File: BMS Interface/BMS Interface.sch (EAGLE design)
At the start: 23 parts

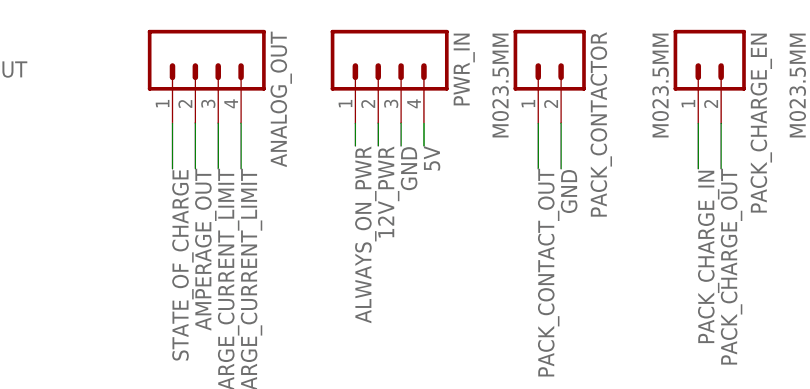
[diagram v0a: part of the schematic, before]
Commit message: Updating layout for BMS interface PCB and removed 5V input as it was no longer necessary.
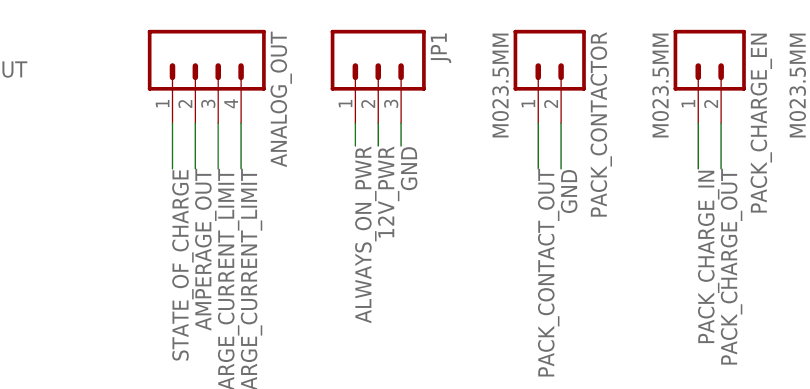
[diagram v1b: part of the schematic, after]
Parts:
- removed PWR_IN: (no value), SparkFun-Connectors:M04SCREW
- added JP1: (no value), SparkFun-Connectors:M03SCREW
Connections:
- removed net 5V: PWR_IN.4
- net 12V_PWR: now also JP1.2; no longer PWR_IN.2
- net ALWAYS_ON_PWR: now also JP1.1; no longer PWR_IN.1
- net GND: now also JP1.3; no longer PWR_IN.3
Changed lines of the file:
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@@
 <parts>
 <part name="BMS_IO" library="SparkFun-Connectors" deviceset="M13X2" device="2X13"/>
-<part name="PWR_IN" library="SparkFun-Connectors" deviceset="M04" device="SCREW"/>
 <part name="CAN1" library="SparkFun-Connectors" deviceset="DB9" device="FEMALE"/>
 <part name="CAN2" library="SparkFun-Connectors" deviceset="DB9" device="FEMALE"/>
@@
 <part name="STANDOFF3" library="SparkFun-Electromechanical" deviceset="STAND-OFF" device=""/>
 <part name="STANDOFF4" library="SparkFun-Electromechanical" deviceset="STAND-OFF" device=""/>
+<part name="JP1" library="SparkFun-Connectors" deviceset="M03" device="SCREW"/>
 </parts>
 <sheets>
@@
 <instances>
 <instance part="BMS_IO" gate="G$1" x="-2.54" y="50.8"/>
-<instance part="PWR_IN" gate="G$1" x="86.36" y="121.92" rot="R270"/>
 <instance part="CAN1" gate="G$1" x="124.46" y="43.18"/>
 <instance part="CAN2" gate="G$1" x="124.46" y="15.24"/>
@@
 <instance part="STANDOFF3" gate="G$1" x="160.02" y="68.58"/>
 <instance part="STANDOFF4" gate="G$1" x="160.02" y="71.12"/>
+<instance part="JP1" gate="G$1" x="86.36" y="124.46" rot="R270"/>
 </instances>
 <busses>
@@
 <wire x1="83.82" y1="116.84" x2="83.82" y2="114.3" width="0.2032" layer="91"/>
 <label x="83.82" y="114.3" size="1.778" layer="95" rot="R270"/>
-<pinref part="PWR_IN" gate="G$1" pin="1"/>
+<pinref part="JP1" gate="G$1" pin="1"/>
 </segment>
 </net>
@@
 <wire x1="88.9" y1="116.84" x2="88.9" y2="114.3" width="0.2032" layer="91"/>
 <label x="88.9" y="114.3" size="1.778" layer="95" rot="R270"/>
-<pinref part="PWR_IN" gate="G$1" pin="3"/>
+<pinref part="JP1" gate="G$1" pin="3"/>
 </segment>
 <segment>
@@
 <wire x1="86.36" y1="116.84" x2="86.36" y2="114.3" width="0.2032" layer="91"/>
 <label x="86.36" y="114.3" size="1.778" layer="95" rot="R270"/>
-<pinref part="PWR_IN" gate="G$1" pin="2"/>
+<pinref part="JP1" gate="G$1" pin="2"/>
 </segment>
 <segment>
@@
 </segment>
 </net>
-<net name="5V" class="0">
-<segment>
-<pinref part="PWR_IN" gate="G$1" pin="4"/>
-<wire x1="91.44" y1="116.84" x2="91.44" y2="114.3" width="0.2032" layer="91"/>
-<label x="91.44" y="114.3" size="1.778" layer="95" rot="R270"/>
-</segment>
-</net>

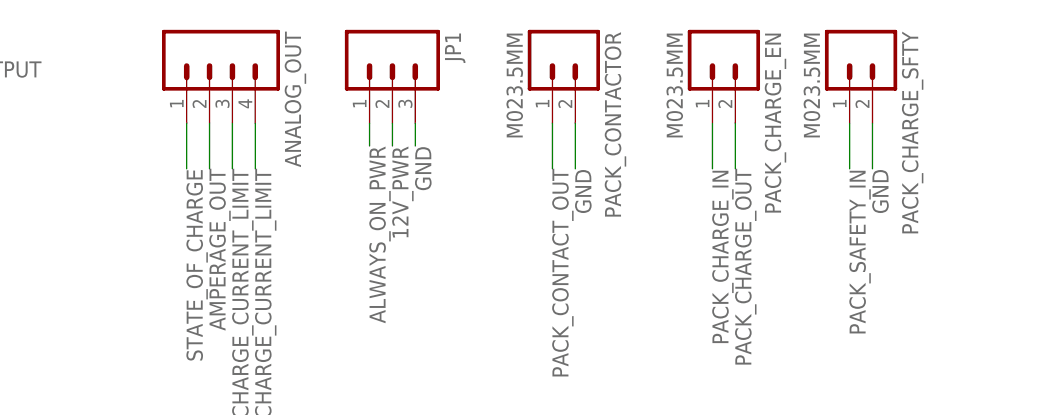
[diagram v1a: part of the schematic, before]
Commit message: CHanged all connectors on MCB to use Molex
Changed most of the connectors on the BMS interface to use molex as
well.
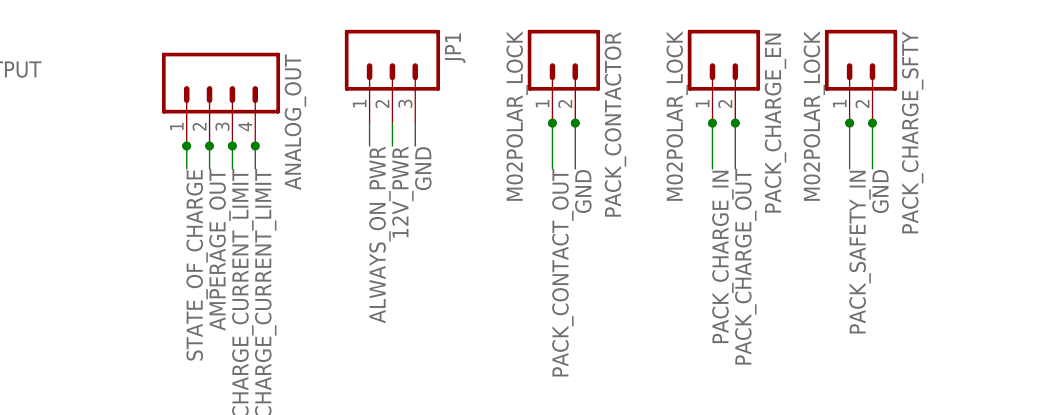
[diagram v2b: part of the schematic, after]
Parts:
- ANALOG_OUT: device SparkFun-Connectors:M04PTH -> SparkFun-Connectors:M04POLAR_LOCK
- PACK_CHARGE_EN, PACK_CHARGE_SFTY, PACK_CONTACTOR: value M023.5MM -> M02POLAR_LOCK; device SparkFun-Connectors:M023.5MM -> SparkFun-Connectors:M02POLAR_LOCK
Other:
- moved on the sheet: ANALOG_OUT
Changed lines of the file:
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@@
 <part name="U$1" library="SparkFun-Electromechanical" deviceset="RELAY-2" device="G5Q"/>
 <part name="U$2" library="SparkFun-Electromechanical" deviceset="RELAY-2" device="G5Q"/>
-<part name="PACK_CONTACTOR" library="SparkFun-Connectors" deviceset="M02" device="3.5MM"/>
 <part name="D1" library="SparkFun-DiscreteSemi" deviceset="DIODE" device="SMA" value="1n4001"/>
-<part name="PACK_CHARGE_EN" library="SparkFun-Connectors" deviceset="M02" device="3.5MM"/>
-<part name="PACK_CHARGE_SFTY" library="SparkFun-Connectors" deviceset="M02" device="3.5MM"/>
 <part name="D2" library="SparkFun-DiscreteSemi" deviceset="DIODE" device="SMA" value="1n4001"/>
 <part name="U$3" library="SparkFun-Electromechanical" deviceset="RELAY-2" device="G5Q"/>
@@
 <part name="FAULT" library="SparkFun-LED" deviceset="LED" device="5MM" value="Red"/>
 <part name="PWR" library="SparkFun-LED" deviceset="LED" device="5MM" value="GREEN"/>
-<part name="ANALOG_OUT" library="SparkFun-Connectors" deviceset="M04" device="PTH"/>
 <part name="STANDOFF1" library="SparkFun-Electromechanical" deviceset="STAND-OFF" device=""/>
 <part name="STANDOFF2" library="SparkFun-Electromechanical" deviceset="STAND-OFF" device=""/>
@@
 <part name="STANDOFF4" library="SparkFun-Electromechanical" deviceset="STAND-OFF" device=""/>
 <part name="JP1" library="SparkFun-Connectors" deviceset="M03" device="SCREW"/>
+<part name="ANALOG_OUT" library="SparkFun-Connectors" deviceset="M04" device="POLAR_LOCK"/>
+<part name="PACK_CONTACTOR" library="SparkFun-Connectors" deviceset="M02" device="POLAR_LOCK"/>
+<part name="PACK_CHARGE_EN" library="SparkFun-Connectors" deviceset="M02" device="POLAR_LOCK"/>
+<part name="PACK_CHARGE_SFTY" library="SparkFun-Connectors" deviceset="M02" device="POLAR_LOCK"/>
 </parts>
 <sheets>
@@
 <instance part="U$1" gate="G$1" x="38.1" y="-2.54" rot="R90"/>
 <instance part="U$2" gate="G$1" x="63.5" y="-2.54" rot="R90"/>
-<instance part="PACK_CONTACTOR" gate="G$1" x="104.14" y="124.46" rot="R270"/>
 <instance part="D1" gate="G$1" x="63.5" y="-17.78" rot="R180"/>
-<instance part="PACK_CHARGE_EN" gate="G$1" x="121.92" y="124.46" rot="R270"/>
-<instance part="PACK_CHARGE_SFTY" gate="G$1" x="137.16" y="124.46" rot="R270"/>
 <instance part="D2" gate="G$1" x="38.1" y="-17.78" rot="R180"/>
 <instance part="U$3" gate="G$1" x="7.62" y="-2.54" rot="R90"/>
@@
 <instance part="FAULT" gate="G$1" x="10.16" y="121.92" rot="R90"/>
 <instance part="PWR" gate="G$1" x="10.16" y="109.22" rot="R90"/>
-<instance part="ANALOG_OUT" gate="G$1" x="66.04" y="121.92" rot="R270"/>
 <instance part="STANDOFF1" gate="G$1" x="162.56" y="71.12"/>
 <instance part="STANDOFF2" gate="G$1" x="162.56" y="68.58"/>
@@
 <instance part="STANDOFF4" gate="G$1" x="160.02" y="71.12"/>
 <instance part="JP1" gate="G$1" x="86.36" y="124.46" rot="R270"/>
+<instance part="ANALOG_OUT" gate="G$1" x="66.04" y="119.38" rot="R270"/>
+<instance part="PACK_CONTACTOR" gate="G$1" x="104.14" y="124.46" rot="R270"/>
+<instance part="PACK_CHARGE_EN" gate="G$1" x="121.92" y="124.46" rot="R270"/>
+<instance part="PACK_CHARGE_SFTY" gate="G$1" x="137.16" y="124.46" rot="R270"/>
 </instances>
 <busses>
@@
 </segment>
 <segment>
+<wire x1="68.58" y1="114.3" x2="68.58" y2="111.76" width="0.2032" layer="91"/>
+<label x="68.58" y="111.76" size="1.778" layer="95" rot="R270"/>
 <pinref part="ANALOG_OUT" gate="G$1" pin="3"/>
-<wire x1="68.58" y1="116.84" x2="68.58" y2="111.76" width="0.2032" layer="91"/>
-<label x="68.58" y="111.76" size="1.778" layer="95" rot="R270"/>
+<junction x="68.58" y="114.3"/>
 </segment>
 </net>
@@
 </segment>
 <segment>
-<pinref part="PACK_CONTACTOR" gate="G$1" pin="2"/>
 <wire x1="106.68" y1="116.84" x2="106.68" y2="111.76" width="0.2032" layer="91"/>
 <label x="106.68" y="111.76" size="1.778" layer="95" rot="R270"/>
-</segment>
-<segment>
-<pinref part="PACK_CHARGE_SFTY" gate="G$1" pin="2"/>
+<pinref part="PACK_CONTACTOR" gate="G$1" pin="2"/>
+<junction x="106.68" y="116.84"/>
+</segment>
+<segment>
 <wire x1="139.7" y1="116.84" x2="139.7" y2="111.76" width="0.2032" layer="91"/>
 <label x="139.7" y="111.76" size="1.778" layer="95" rot="R270"/>
+<pinref part="PACK_CHARGE_SFTY" gate="G$1" pin="2"/>
+<junction x="139.7" y="116.84"/>
 </segment>
 <segment>
@@
 </segment>
 <segment>
+<wire x1="66.04" y1="114.3" x2="66.04" y2="111.76" width="0.2032" layer="91"/>
+<label x="66.04" y="111.76" size="1.778" layer="95" rot="R270"/>
 <pinref part="ANALOG_OUT" gate="G$1" pin="2"/>
-<wire x1="66.04" y1="116.84" x2="66.04" y2="111.76" width="0.2032" layer="91"/>
-<label x="66.04" y="111.76" size="1.778" layer="95" rot="R270"/>
+<junction x="66.04" y="114.3"/>
 </segment>
 </net>
@@
 </segment>
 <segment>
+<wire x1="63.5" y1="114.3" x2="63.5" y2="111.76" width="0.2032" layer="91"/>
+<label x="63.5" y="111.76" size="1.778" layer="95" rot="R270"/>
 <pinref part="ANALOG_OUT" gate="G$1" pin="1"/>
-<wire x1="63.5" y1="116.84" x2="63.5" y2="111.76" width="0.2032" layer="91"/>
-<label x="63.5" y="111.76" size="1.778" layer="95" rot="R270"/>
+<junction x="63.5" y="114.3"/>
 </segment>
 </net>
@@
 </segment>
 <segment>
+<wire x1="71.12" y1="114.3" x2="71.12" y2="111.76" width="0.2032" layer="91"/>
+<label x="71.12" y="111.76" size="1.778" layer="95" rot="R270"/>
 <pinref part="ANALOG_OUT" gate="G$1" pin="4"/>
-<wire x1="71.12" y1="116.84" x2="71.12" y2="111.76" width="0.2032" layer="91"/>
-<label x="71.12" y="111.76" size="1.778" layer="95" rot="R270"/>
+<junction x="71.12" y="114.3"/>
 </segment>
 </net>
@@
 <net name="PACK_CONTACT_OUT" class="0">
 <segment>
-<pinref part="PACK_CONTACTOR" gate="G$1" pin="1"/>
 <wire x1="104.14" y1="116.84" x2="104.14" y2="111.76" width="0.2032" layer="91"/>
 <label x="104.14" y="111.76" size="1.778" layer="95" rot="R270"/>
+<pinref part="PACK_CONTACTOR" gate="G$1" pin="1"/>
+<junction x="104.14" y="116.84"/>
 </segment>
 <segment>
@@
 <net name="PACK_CHARGE_IN" class="0">
 <segment>
-<pinref part="PACK_CHARGE_EN" gate="G$1" pin="1"/>
 <wire x1="121.92" y1="116.84" x2="121.92" y2="111.76" width="0.2032" layer="91"/>
 <label x="121.92" y="111.76" size="1.778" layer="95" rot="R270"/>
+<pinref part="PACK_CHARGE_EN" gate="G$1" pin="1"/>
+<junction x="121.92" y="116.84"/>
 </segment>
 <segment>
@@
 <net name="PACK_CHARGE_OUT" class="0">
 <segment>
-<pinref part="PACK_CHARGE_EN" gate="G$1" pin="2"/>
 <wire x1="124.46" y1="116.84" x2="124.46" y2="111.76" width="0.2032" layer="91"/>
 <label x="124.46" y="111.76" size="1.778" layer="95" rot="R270"/>
+<pinref part="PACK_CHARGE_EN" gate="G$1" pin="2"/>
+<junction x="124.46" y="116.84"/>
 </segment>
 <segment>
@@
 <net name="PACK_SAFETY_IN" class="0">
 <segment>
-<pinref part="PACK_CHARGE_SFTY" gate="G$1" pin="1"/>
 <wire x1="137.16" y1="116.84" x2="137.16" y2="111.76" width="0.2032" layer="91"/>
 <label x="137.16" y="111.76" size="1.778" layer="95" rot="R270"/>
-</segment>
-<segment>
+<pinref part="PACK_CHARGE_SFTY" gate="G$1" pin="1"/>
+<junction x="137.16" y="116.84"/>
+</segment>
+<segment>

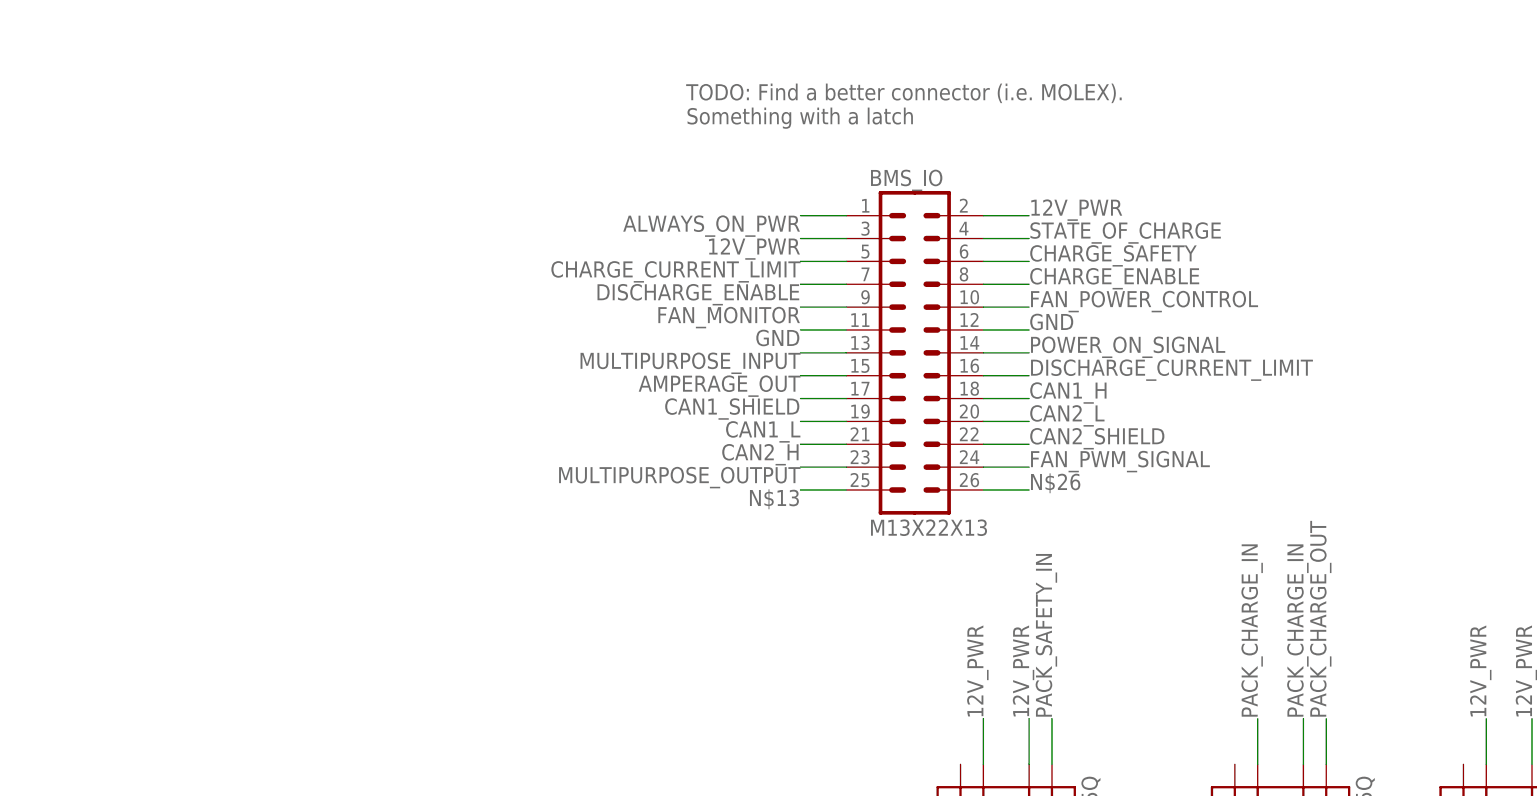
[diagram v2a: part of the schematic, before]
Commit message: Moved BMS interface to use an ATX connector.
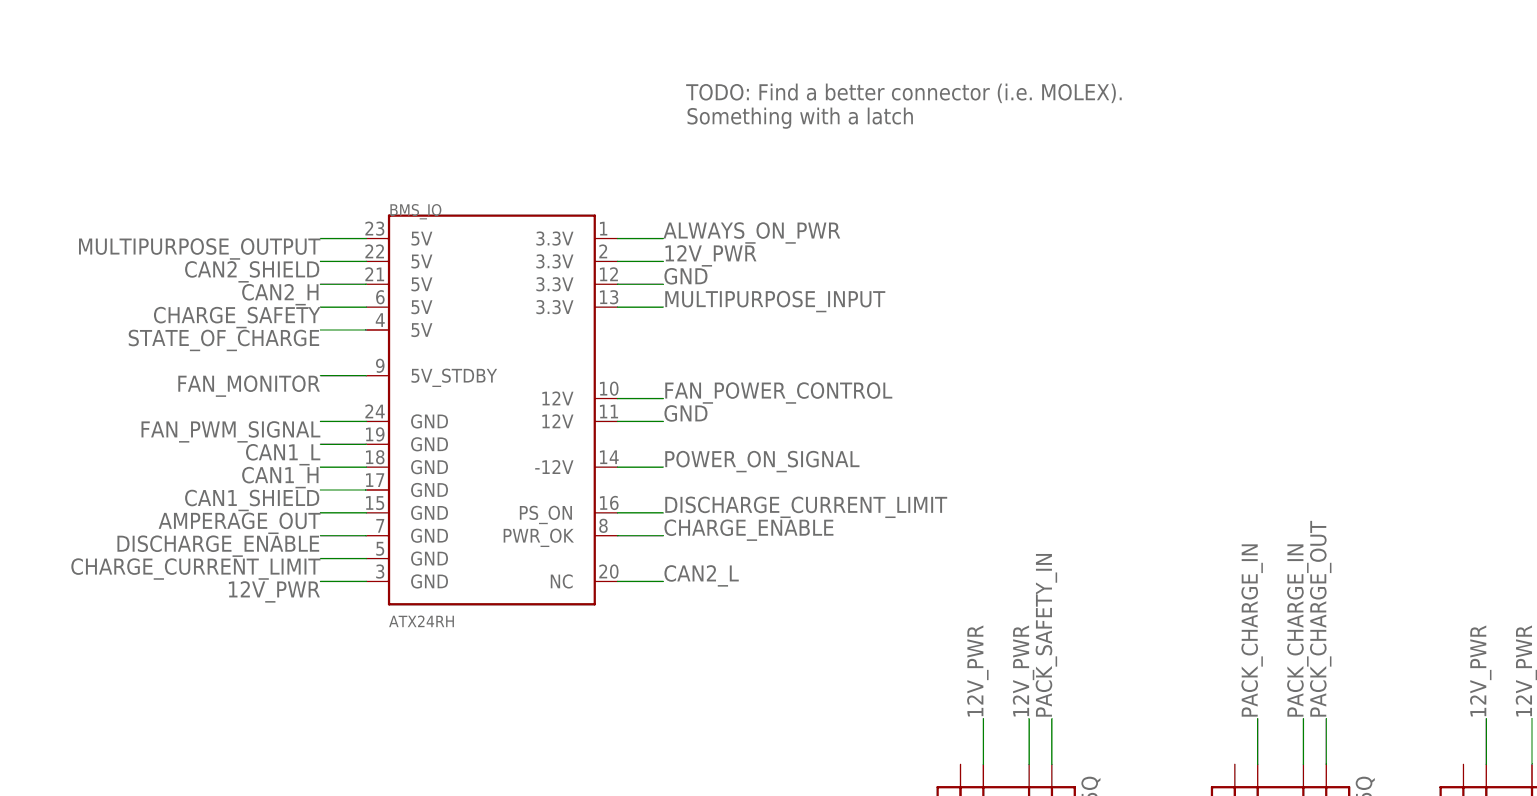
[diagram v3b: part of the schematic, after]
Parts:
- BMS_IO: value M13X22X13 -> ATX24RH; device SparkFun-Connectors:M13X22X13 -> SparkFun-Connectors:ATX24RH
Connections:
- removed net N$13: BMS_IO.25
- removed net N$26: BMS_IO.26
- net 12V_PWR: now also BMS_IO.3.3V@1, BMS_IO.GND@0; no longer BMS_IO.2, BMS_IO.3
- net ALWAYS_ON_PWR: now also BMS_IO.3.3V@0; no longer BMS_IO.1
- net AMPERAGE_OUT: now also BMS_IO.GND@3; no longer BMS_IO.15
- net CAN1_H: now also BMS_IO.GND@5; no longer BMS_IO.18
- net CAN1_L: now also BMS_IO.GND@6; no longer BMS_IO.19
- net CAN1_SHIELD: now also BMS_IO.GND@4; no longer BMS_IO.17
- net CAN2_H: now also BMS_IO.5V@2; no longer BMS_IO.21
- net CAN2_L: now also BMS_IO.NC; no longer BMS_IO.20
- net CAN2_SHIELD: now also BMS_IO.5V@3; no longer BMS_IO.22
- net CHARGE_CURRENT_LIMIT: now also BMS_IO.GND@1; no longer BMS_IO.5
- net CHARGE_ENABLE: now also BMS_IO.PWR_OK; no longer BMS_IO.8
- net CHARGE_SAFETY: now also BMS_IO.5V@1; no longer BMS_IO.6
- net DISCHARGE_CURRENT_LIMIT: now also BMS_IO.PS_ON; no longer BMS_IO.16
- net DISCHARGE_ENABLE: now also BMS_IO.GND@2; no longer BMS_IO.7
- net FAN_MONITOR: now also BMS_IO.5V_STDBY; no longer BMS_IO.9
- net FAN_POWER_CONTROL: now also BMS_IO.12V@0; no longer BMS_IO.10
- net FAN_PWM_SIGNAL: now also BMS_IO.GND@7; no longer BMS_IO.24
- net GND: now also BMS_IO.12V@1, BMS_IO.3.3V@2; no longer BMS_IO.11, BMS_IO.12
- net MULTIPURPOSE_INPUT: now also BMS_IO.3.3V@3; no longer BMS_IO.13
- net MULTIPURPOSE_OUTPUT: now also BMS_IO.5V@4; no longer BMS_IO.23
- net POWER_ON_SIGNAL: now also BMS_IO.-12V; no longer BMS_IO.14
- net STATE_OF_CHARGE: now also BMS_IO.5V@0; no longer BMS_IO.4

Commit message: UPdating resistor packages to sizes which are
capable of disappating the appropriate amount of power.
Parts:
- R3: device SparkFun-Resistors:RESISTOR0603 -> SparkFun-Passives:RESISTOR0805-RES
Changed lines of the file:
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@@
 <part name="U$3" library="SparkFun-Electromechanical" deviceset="RELAY-2" device="G5Q"/>
 <part name="D3" library="SparkFun-DiscreteSemi" deviceset="DIODE" device="SMA" value="1n4001"/>
-<part name="R3" library="SparkFun-Resistors" deviceset="RESISTOR" device="0603" value="1K"/>
 <part name="FAULT" library="SparkFun-LED" deviceset="LED" device="5MM" value="Red"/>
 <part name="PWR" library="SparkFun-LED" deviceset="LED" device="5MM" value="GREEN"/>
@@
 <part name="PACK_CHARGE_SFTY" library="SparkFun-Connectors" deviceset="M02" device="POLAR_LOCK"/>
 <part name="BMS_IO" library="SparkFun-Connectors" deviceset="ATX24" device="RH"/>
+<part name="R3" library="SparkFun-Passives" deviceset="RESISTOR" device="0805-RES" value="1K"/>
 </parts>
 <sheets>
@@
 <instance part="U$3" gate="G$1" x="7.62" y="-2.54" rot="R90"/>
 <instance part="D3" gate="G$1" x="7.62" y="-17.78" rot="R180"/>
-<instance part="R3" gate="G$1" x="-5.08" y="121.92"/>
 <instance part="FAULT" gate="G$1" x="10.16" y="121.92" rot="R90"/>
 <instance part="PWR" gate="G$1" x="10.16" y="109.22" rot="R90"/>
@@
 <instance part="PACK_CHARGE_SFTY" gate="G$1" x="137.16" y="124.46" rot="R270"/>
 <instance part="BMS_IO" gate="G$1" x="-48.26" y="45.72"/>
+<instance part="R3" gate="G$1" x="-5.08" y="121.92"/>
 </instances>
 <busses>
@@
 </segment>
 <segment>
-<pinref part="R3" gate="G$1" pin="1"/>
 <wire x1="-10.16" y1="121.92" x2="-20.32" y2="121.92" width="0.2032" layer="91"/>
 <label x="-20.32" y="121.92" size="1.778" layer="95" rot="R180"/>
+<pinref part="R3" gate="G$1" pin="1"/>
 </segment>
 <segment>
@@
 <net name="N$2" class="0">
 <segment>
-<pinref part="R3" gate="G$1" pin="2"/>
 <pinref part="FAULT" gate="G$1" pin="A"/>
 <wire x1="0" y1="121.92" x2="7.62" y2="121.92" width="0.2032" layer="91"/>
-</segment>
-</net>
+<pinref part="R3" gate="G$1" pin="2"/>
+</segment>
+</net>
